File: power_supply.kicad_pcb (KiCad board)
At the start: 2 copper layers, 85 x 56 mm, 24 parts, among them J1 12v, 2A, J2 Screw_Terminal_01x02, J3 Fan, J4 Conn_01x05, M1 U3V70F5, M2 D24V50F5, U1 ALD910027, U2 MCP9700A-E_TO, U3 PIC12F1840-ISN

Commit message: Version 1.0 includes fixes/changes and FRAM support
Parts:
- added C3: 2.2uF Tant, Capacitor_Tantalum_SMD:CP_EIA-3216-18_Kemet-A, B.Cu at (118.4, 115.8)
- added C4: 2.2uF Tant, Capacitor_Tantalum_SMD:CP_EIA-3216-18_Kemet-A, B.Cu at (118.4, 121.2)
- added C5: 1uF, Capacitor_SMD:C_1206_3216Metric_Pad1.33x1.80mm_HandSolder, B.Cu at (136.7, 128.5)
- added C6: 1uF, Capacitor_SMD:C_1206_3216Metric_Pad1.33x1.80mm_HandSolder, B.Cu at (142.1, 128.5)
- added D10: PWRUP, Diode_SMD:D_1206_3216Metric_Castellated, B.Cu at (95.0, 111.0)
- added D4: FAULT, Diode_SMD:D_1206_3216Metric_Castellated, B.Cu at (95.0, 117.0)
- added D5: V8PAM10S, Footprint_Library:DO-221BC, B.Cu at (171.8, 119.5)
- added D6: MAINPWR, Diode_SMD:D_1206_3216Metric_Castellated, B.Cu at (95.0, 105.0)
- added D7: BAT54SW, Package_TO_SOT_SMD:SOT-323_SC-70, B.Cu at (173.7, 97.3)
- added D8: Activity, Diode_SMD:D_1206_3216Metric_Castellated, B.Cu at (95.0, 93.0)
- added D9: V8PAM10S, Footprint_Library:DO-221BC, B.Cu at (175.8, 116.6)
- added G***: LOGO, Crius:Crius_logo_36x9mm, B.Cu at (170.4, 86.8)
- added G***: LOGO, Crius:Crius_logo_20x5mm, F.Cu at (180.1, 130.7)
- added J5: Program, Connector_PinHeader_2.54mm:PinHeader_1x05_P2.54mm_Vertical, F.Cu at (121.0, 107.8)
- added J6: Serial Debug, Connector_PinHeader_2.54mm:PinHeader_1x02_P2.54mm_Vertical, F.Cu at (124.7, 107.9)
- added J7: REMOVE to PRGM, Connector_PinHeader_2.54mm:PinHeader_1x02_P2.54mm_Vertical, F.Cu at (122.7, 114.8)
- added J8: 5V 25W, Connectors:Screw_Terminal_2Pin, F.Cu at (166.9, 132.7)
- added J9: FRAM I2C, Connector_JST:JST_XH_B3B-XH-A_1x03_P2.50mm_Vertical, F.Cu at (127.5, 127.9)
- added M3: U3V70F5, Pololu:U3V70F5, F.Cu at (166.2, 120.4)
- added Q1: BSS806, digikey-footprints:SOT-23-3, B.Cu at (138.1, 84.5)
- added Q2: BSS806, digikey-footprints:SOT-23-3, B.Cu at (148.5, 96.6)
- added Q3: SPD18P06PGBTMA1, Package_TO_SOT_SMD:TO-252-3_TabPin2, B.Cu at (126.3, 91.1)
- added Q4: BSS806, digikey-footprints:SOT-23-3, B.Cu at (162.0, 125.4)
- added Q5: BSS806, digikey-footprints:SOT-23-3, B.Cu at (115.9, 125.2)
- added Q6: SQ3495-EV, digikey-footprints:SOT-23-6, B.Cu at (180.9, 107.8)
- added R10: 1R 25W, Connector_Wire:SolderWire-0.5sqmm_1x02_P4.6mm_D0.9mm_OD2.1mm, F.Cu at (152.9, 110.1)
- added R11: 1k, Resistor_SMD:R_1206_3216Metric, B.Cu at (100.0, 106.5)
- added R12: 10k, Resistor_SMD:R_1206_3216Metric, B.Cu at (109.7, 88.2)
- added R13: 9k 0.1%, Resistor_SMD:R_1206_3216Metric, B.Cu at (106.1, 91.9)
- added R14: 1k, Resistor_SMD:R_1206_3216Metric, B.Cu at (100.1, 94.4)
- added R15: 9k 0.1%, Resistor_SMD:R_1206_3216Metric, B.Cu at (111.3, 94.5)
- added R16: 1k 0.1%, Resistor_SMD:R_1206_3216Metric, B.Cu at (106.0, 94.6)
- added R17: 9k 0.1%, Resistor_SMD:R_1206_3216Metric, B.Cu at (116.8, 94.8)
- added R18: 10k, Resistor_SMD:R_1206_3216Metric, B.Cu at (175.6, 102.1)
- added R19: 1k 0.1%, Resistor_SMD:R_1206_3216Metric, B.Cu at (111.3, 91.9)
- added R20: 1k 0.1%, Resistor_SMD:R_1206_3216Metric, B.Cu at (116.8, 91.8)
- added R21: 1k, Resistor_SMD:R_1206_3216Metric, B.Cu at (100.0, 112.4)
- added R22: 50, Resistor_SMD:R_1206_3216Metric, B.Cu at (118.4, 118.4)
- added R23: 10k, Resistor_SMD:R_1206_3216Metric, B.Cu at (132.3, 123.3)
- added R24: 10k, Resistor_SMD:R_1206_3216Metric, B.Cu at (130.0, 123.3)
- added R5: 1k, Resistor_SMD:R_1206_3216Metric, B.Cu at (168.2, 124.4)
- added R6: 1k, Resistor_SMD:R_1206_3216Metric, B.Cu at (100.0, 118.4)
- added R7: 1k 0.1%, Resistor_SMD:R_1206_3216Metric, B.Cu at (107.3, 119.4)
- added R8: 1k 0.1%, Resistor_SMD:R_1206_3216Metric, B.Cu at (112.7, 119.4)
- added R9: 10k, Resistor_SMD:R_1206_3216Metric, B.Cu at (115.7, 109.8)
- added S1: RESET, digikey-footprints:Switch_Tactile_SMD_6x6mm, B.Cu at (109.7, 114.6)
- added U4: PIC16F1709, Package_SO:SOIC-20W_7.5x12.8mm_P1.27mm, B.Cu at (109.9, 102.5)
- added U5: MCP111-195, digikey-footprints:SOT-23-3, B.Cu at (142.1, 108.5)
- added U6: MB85RC1MT, Package_SO:SOIC-8_3.9x4.9mm_P1.27mm, B.Cu at (137.4, 123.8)
- added U7: MCP1700-3302E_SOT23, Package_TO_SOT_SMD:SOT-23, B.Cu at (143.0, 123.2)
- added VRef1: MCP1501-6Pin, digikey-footprints:SOT-23-6, B.Cu at (118.4, 112.8)
- C1: value .1 -> 100uF; footprint Capacitor_SMD:C_1206_3216Metric_Pad1.42x1.75mm_HandSolder -> Capacitor_SMD:CP_Elec_6.3x5.2; moved to B.Cu
- C2: footprint Capacitor_SMD:C_1206_3216Metric_Pad1.42x1.75mm_HandSolder -> Capacitor_SMD:C_1206_3216Metric_Pad1.33x1.80mm_HandSolder; moved to B.Cu
- D1, D2: value 1N5817 -> 1N914; footprint Diode_THT:D_DO-41_SOD81_P10.16mm_Horizontal -> Diode_SMD:D_SOD-123F; moved to B.Cu
- D3: value LED -> ShutDown; moved to B.Cu
- J1: value 12v, 2A -> 12v, 0.5A nominal, 5A Surge
- J2: value Screw_Terminal_01x02 -> Power Switch; footprint Connectors:Screw_Terminal_2Pin -> Connector_JST:JST_XH_B5B-XH-A_1x05_P2.50mm_Vertical
- J3: value Fan -> Shutdown
- J4: value Conn_01x05 -> 12V 5V; footprint Connector_PinHeader_2.54mm:PinHeader_1x05_P2.54mm_Vertical -> Connector_PinHeader_2.54mm:PinHeader_1x03_P2.54mm_Vertical
- M1: value U3V70F5 -> XL4015; footprint Pololu Regulators:U3V70F5 -> Footprint_Library:XL4015
- M2: value D24V50F5 -> U1V11F5; footprint Pololu Regulators:D24V50F5 -> Pololu:U1V11Fx
- R1: value 1k -> 10k; moved to B.Cu
- R2: value 10k -> 1k; moved to B.Cu
- R3, R4: moved to B.Cu
- SC1, SC2: value SuperCap -> 100F/200F; footprint SuperCaps:SCC-30mm -> SuperCaps:SCC-22-30mm
- U1: value ALD910027 -> MCP9700A; footprint Package_SO:SOIC-8_3.9x4.9mm_P1.27mm -> digikey-footprints:SOT-23-3; moved to B.Cu
- U2: value MCP9700A-E_TO -> BTS443P; footprint digikey-footprints:TO-92-3 -> Package_TO_SOT_SMD:TO-252-4; moved to B.Cu
- U3: value PIC12F1840-ISN -> ALD910027; footprint Package_SO:SO-8_3.9x4.9mm_P1.27mm -> Package_SO:SOIC-8_3.9x4.9mm_P1.27mm; moved to B.Cu
- moved U1 85.0 mm to (96.2, 128.0)
- moved J2 58.4 mm to (148.7, 131.3), turned to 0 degrees
- moved J1 57.4 mm to (140.2, 132.7)
- moved J3 56.2 mm to (121.2, 124.3), turned to 0 degrees
- moved U3 55.1 mm to (181.1, 97.7), turned to 0 degrees
- moved D1 52.2 mm to (114.7, 88.2), turned to 180 degrees
- moved D2 42.8 mm to (132.9, 85.7)
- moved D3 40.1 mm to (95.0, 99.0), turned to 270 degrees
- moved SC2 38.7 mm to (139.8, 97.0)
- moved R2 38.3 mm to (109.1, 129.6), turned to 0 degrees
- moved U2 37.8 mm to (162.1, 119.5), turned to 0 degrees
- moved J4 34.7 mm to (152.5, 83.4)
- moved R3 33.1 mm to (100.0, 100.4), turned to 180 degrees
- moved SC1 22.4 mm to (170.3, 97.0), turned to 180 degrees
- moved R4 14.8 mm to (124.9, 99.0)
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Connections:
- C1 pad 1: /5V -> Net-(C1-Pad1)
- C1 pad 2: /GND -> Net-(C1-Pad2)
- C2 pad 1: /GND -> Net-(C1-Pad2)
- C2 pad 2: /5V -> Net-(C1-Pad1)
- D1 pad 1: /2.5-5V -> Net-(D1-Pad1)
- D2 pad 1: Net-(D1-Pad2) -> Net-(D1-Pad1)
- D2 pad 2: /GND -> Net-(D2-Pad2)
- D3 pad 1: /GND -> Net-(C1-Pad2)
- J1 pad 1: /GND -> Net-(C1-Pad2)
- J1 pad 2: /12v -> Net-(J1-Pad2)
- J2 pad 1: /GND -> Net-(C1-Pad2)
- J2 pad 2: /5V -> Net-(D1-Pad1)
- J3 pad 1: /GND -> Net-(C1-Pad2)
- J3 pad 2: /12v -> Net-(J3-Pad2)
- J4 pad 1: Net-(J4-Pad1) -> Net-(J2-Pad3)
- J4 pad 2: /5V -> Net-(J4-Pad2)
- J4 pad 3: /GND -> Net-(D5-Pad2)
- M1 pad 1: Net-(M1-Pad1) -> Net-(J2-Pad3)
- M1 pad 2: /GND -> Net-(C1-Pad2)
- M1 pad 3: /GND -> Net-(C1-Pad2)
- M1 pad 4: /GND -> Net-(D5-Pad2)
- M2 pad 1: Net-(M2-Pad1) -> Net-(C1-Pad1)
- M2 pad 2: /12v -> Net-(C1-Pad2)
- M2 pad 3: /GND -> Net-(D9-Pad1)
- M2 pad 4: /GND -> Net-(M2-Pad4)
- R1 pad 1: Net-(D3-Pad2) -> Net-(D2-Pad2)
- R1 pad 2: Net-(R1-Pad2) -> Net-(J2-Pad3)
- R2 pad 1: /5V -> Net-(R2-Pad1)
- R2 pad 2: Net-(J4-Pad1) -> Net-(Q5-Pad1)
- R3 pad 1: Net-(R3-Pad1) -> Net-(R2-Pad1)
- R3 pad 2: /2.5-5V -> Net-(D3-Pad2)
- R4 pad 1: /GND -> Net-(R4-Pad1)
- R4 pad 2: Net-(R3-Pad1) -> Net-(Q2-Pad1)
- SC1 pad 1: Net-(D1-Pad2) -> Net-(D7-Pad3)
- SC1 pad 2: /2.5-5V -> Net-(D7-Pad2)
- SC2 pad 1: /GND -> Net-(C1-Pad2)
- SC2 pad 2: Net-(D1-Pad2) -> Net-(D7-Pad3)
- U1 pad 1: /GND -> Net-(C1-Pad1)
- U1 pad 2: /2.5-5V -> Net-(R7-Pad2)
- U1 pad 3: /2.5-5V -> Net-(C1-Pad2)
- U2 pad 1: /5V -> Net-(R10-Pad1)
- U2 pad 2: Net-(U2-Pad2) -> Net-(R6-Pad1)
- U2 pad 3: /GND -> Net-(D5-Pad1)
- U3 pad 1: /5V -> Net-(C1-Pad2)
- U3 pad 2: Net-(R3-Pad1) -> Net-(D7-Pad2)
- U3 pad 3: Net-(U2-Pad2) -> Net-(D7-Pad2)
- U3 pad 4: Net-(J4-Pad1) -> Net-(D7-Pad3)
- U3 pad 5: Net-(R1-Pad2) -> Net-(C1-Pad2)
- U3 pad 6: Net-(J4-Pad5) -> Net-(D7-Pad3)
- U3 pad 7: Net-(J4-Pad4) -> Net-(D7-Pad3)
- U3 pad 8: /GND -> Net-(D7-Pad2)
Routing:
- net Net-(C1-Pad2): track 0.00 -> 214.2 mm, vias 0 -> 6
- net Net-(D5-Pad2): track 0.00 -> 179.0 mm, vias 0 -> 1
- net Net-(M3-Pad1): track 0.00 -> 116.2 mm, vias 0 -> 2
- net Net-(C1-Pad1): track 0.00 -> 115.9 mm, vias 0 -> 1
- net Net-(D7-Pad2): track 0.00 -> 102.9 mm
- net Net-(J2-Pad3): track 0.00 -> 101.0 mm, vias 0 -> 4
- net /2.5-5V: track 100.2 -> 0.00 mm
- net Net-(D7-Pad3): track 0.00 -> 89.6 mm, vias 0 -> 1
- net Net-(D1-Pad1): track 0.00 -> 88.5 mm, vias 0 -> 6
- net Net-(R6-Pad1): track 0.00 -> 74.6 mm, vias 0 -> 2
- net /GND: track 73.8 -> 0.00 mm
- net Net-(D9-Pad1): track 0.00 -> 73.5 mm, vias 0 -> 1
- net /5V: track 70.0 -> 0.00 mm
- net Net-(C6-Pad1): track 0.00 -> 61.8 mm
- net Net-(Q1-Pad1): track 0.00 -> 61.3 mm
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- added copper zone on F.Cu, net Net-(C1-Pad2)
- removed copper zone on B.Cu, net /GND
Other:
- board size 85 x 56 mm -> 95 x 56 mm
- board text added: "- 12V +"
- board text added: "- 5V +"
- board text added: "FAN"
- board text added: "INPUT 12V"
- board text added: "INPUT PWR"
- board text added: "LED|5V|12V|SW|GND"
- board text added: "OUTPUT 5V 25W"
- board text added: "OUTPUT PWR"
- board text added: "POWER SW"
- board text added: "Program Port"
- board text added: "SCPS - v1.0"

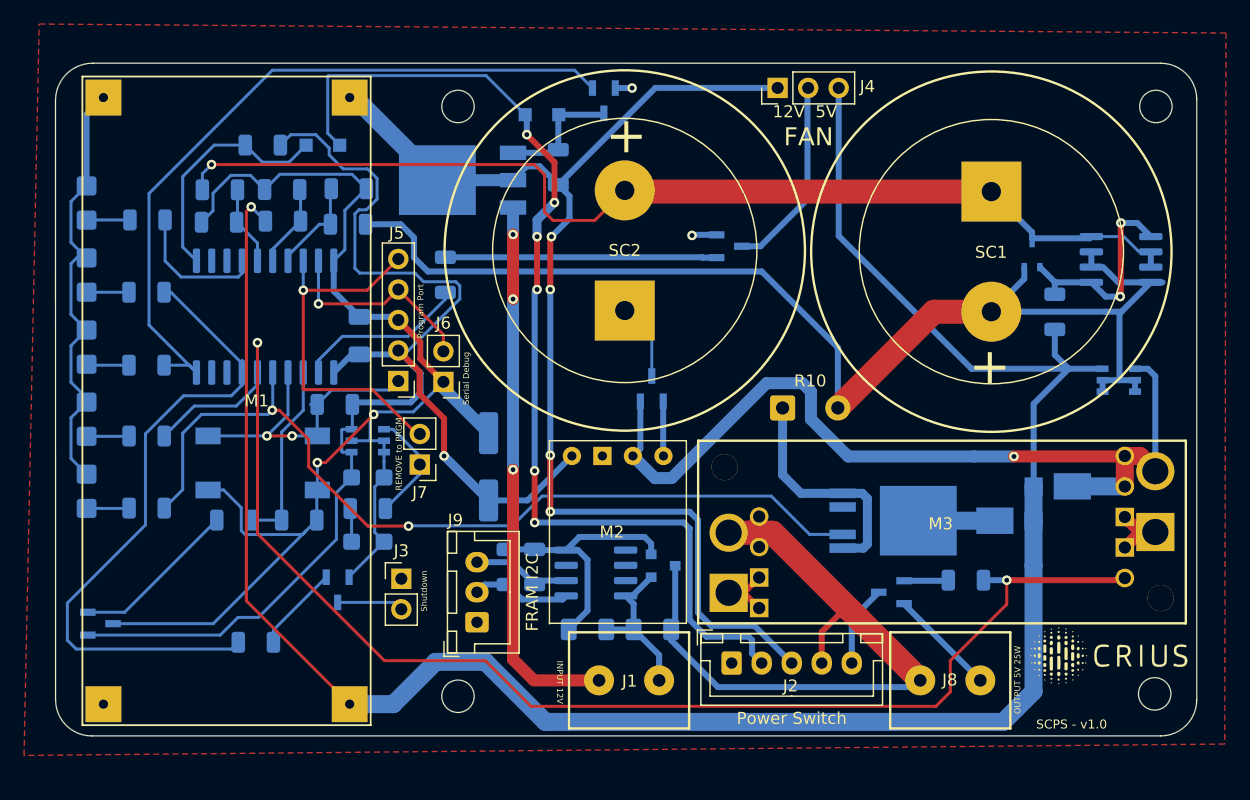
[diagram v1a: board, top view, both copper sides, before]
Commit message: Version 1.01 - Includes fixes, footprint validation, gerbers, screenshots, documentation
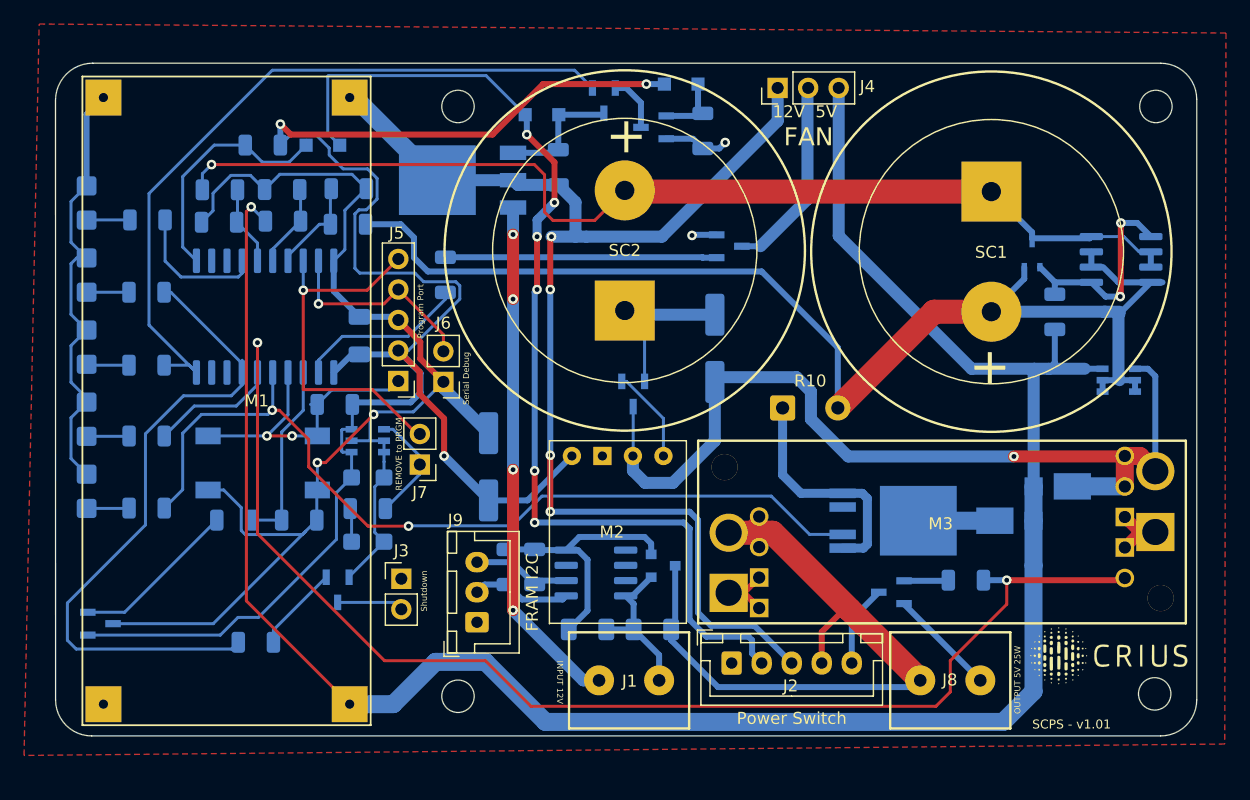
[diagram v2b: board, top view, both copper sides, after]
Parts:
- added C7: 100uF, Capacitor_SMD:CP_Elec_6.3x5.2, B.Cu at (147.3, 105.1)
- added D11: D_Zener, Diode_SMD:D_SOD-123F, B.Cu at (144.5, 83.1)
- added Q7: BSS806, digikey-footprints:SOT-23-3, B.Cu at (142.2, 86.7)
- added R25: 470, Resistor_SMD:R_1206_3216Metric, B.Cu at (146.3, 87.0)
- U5: value MCP111-195 -> MCP111-SOT23
- moved U5 1.61 mm to (140.5, 108.9), turned to 270 degrees
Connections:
- D9 pad 1: Net-(D9-Pad1) -> Net-(C7-Pad1)
- M2 pad 3: Net-(D9-Pad1) -> Net-(C7-Pad1)
- M3 pad 5: Net-(D9-Pad1) -> Net-(C7-Pad1)
- M3 pad 6: Net-(D9-Pad1) -> Net-(C7-Pad1)
- M3 pad 7: Net-(D9-Pad1) -> Net-(C7-Pad1)
- Q1 pad 2: Net-(C1-Pad2) -> Net-(Q1-Pad2)
- Q6 pad 4: Net-(D9-Pad1) -> Net-(C7-Pad1)
- U5 pad 2: Net-(D9-Pad1) -> Net-(C1-Pad2)
- U5 pad 3: Net-(C1-Pad2) -> Net-(C7-Pad1)
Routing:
- net Net-(C7-Pad1): track 0.00 -> 77.2 mm, vias 0 -> 1
- net Net-(D9-Pad1): track 73.5 -> 0.00 mm, vias 1 -> 0
- net Net-(C1-Pad1): track 115.9 -> 151.7 mm, vias 1 -> 3
- net Net-(C1-Pad2): track 214.2 -> 229.3 mm
- net Net-(D11-Pad2): track 0.00 -> 5.76 mm
- net Net-(Q1-Pad2): track 0.00 -> 4.70 mm
- net Net-(M2-Pad4): track 4.57 -> 7.90 mm
- net Net-(J2-Pad3): track 101.0 -> 103.6 mm
- net Net-(J1-Pad2): track 45.5 -> 43.1 mm, vias 3 -> 4
- net Net-(D5-Pad2): track 179.0 -> 177.6 mm
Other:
- board text added: "SCPS - v1.01"
- board text removed: "SCPS - v1.0"
